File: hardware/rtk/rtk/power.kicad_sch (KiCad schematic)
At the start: 28 parts, among them J1 USB4105-GF-A, J3 B2B-PH-SM4-TBLFSN, J4 Conn_01x02_Pin, U1 BQ24075RGT, U2 TPS63020DSJR

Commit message: Schematic fixes and PCB placement start: D2, C16/18/20, J4
- D2: PRTR5V0U2X → USBLC6-2SC6 (SOT-23-6), D3 removed
- C16/C18/C20: symbol → C_Polarized_Small, footprint → 0805 HandSolder
  (T529P106M010AAE200 polymer tant 10µF 10V)
- J4: footprint assigned (PinHeader 2.54mm, on/off switch)
- rtk.kicad_pcb: initial component placement begun
- Add USBLC6-2SC6 datasheet

Co-Authored-By: Claude Sonnet 4.6 <noreply@anthropic.com>
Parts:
- J4: footprint (none) -> Connector_PinHeader_2.54mm:PinHeader_1x02_P2.54mm_Vertical
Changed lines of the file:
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@@
 			)
 		)
-		(property "Footprint" ""
+		(property "Footprint" "Connector_PinHeader_2.54mm:PinHeader_1x02_P2.54mm_Vertical"
 			(at 251.46 55.88 0)
 			(hide yes)

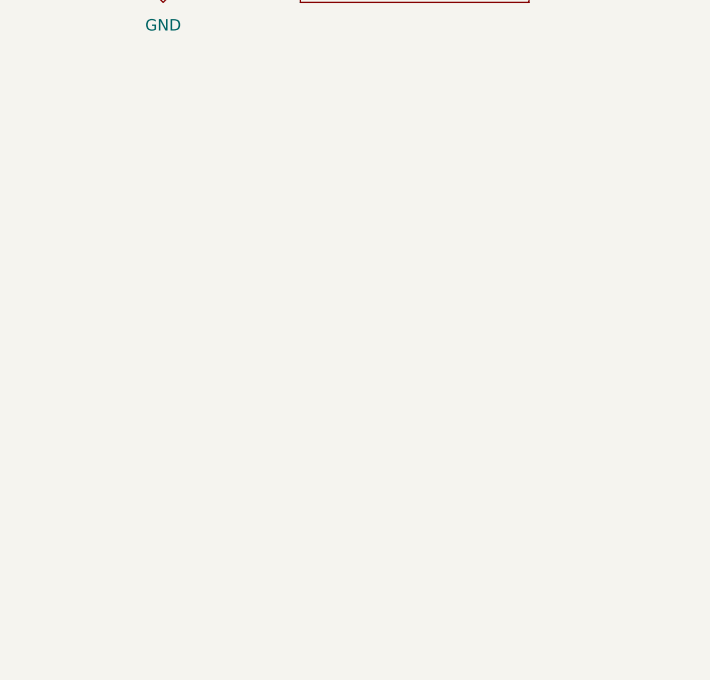
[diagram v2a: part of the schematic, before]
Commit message: Add LD3/LD4 debug LEDs: schematic, PCB placement, ioc
LD3 green PD5, LD4 red PD6 — open-drain outputs, R20/R21 1k5 pull-ups.
CubeMX regenerated with PD5/PD6 configured. Ready for routing.

Co-Authored-By: Claude Sonnet 4.6 <noreply@anthropic.com>
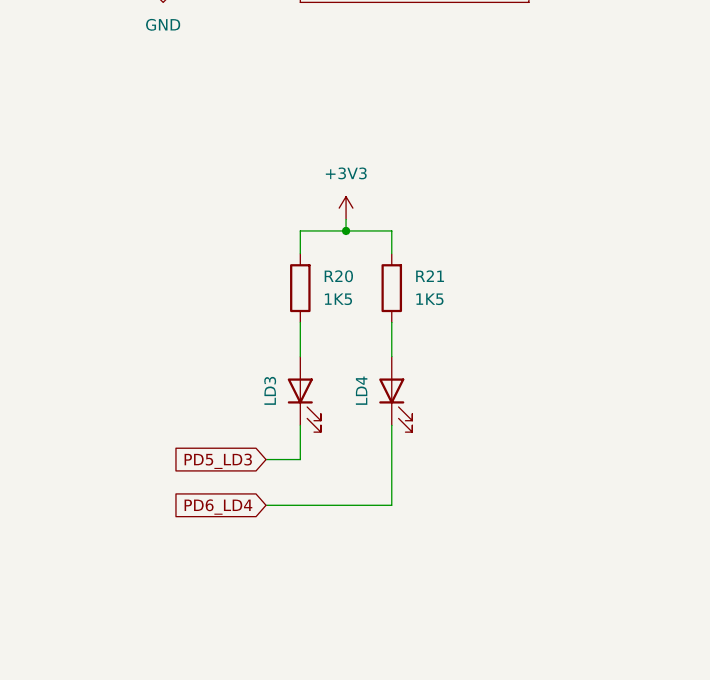
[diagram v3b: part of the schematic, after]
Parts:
- added LD3, LD4: LED, LED_SMD:LED_0805_2012Metric_Pad1.15x1.40mm_HandSolder, symbol Device:LED
- added R20, R21: 1K5, Resistor_SMD:R_0805_2012Metric_Pad1.20x1.40mm_HandSolder, symbol Device:R
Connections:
- net +3V3: now also R20.2, R21.2
- new net: LD4.2 (A), R21.1
- new net: LD3.2 (A), R20.1
- new net PD5_LD3: LD3.1 (K)
- new net PD6_LD4: LD4.1 (K)

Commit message: Add VBAT monitor: 100k divider to PA1 ADC1_IN1
Two 100k resistors divide VBAT by 2 (VBAT_2) fed to PA1. CubeMX
regenerated with ADC1 IN1 on PA1. HAL ADC driver files added.

Co-Authored-By: Claude Sonnet 4.6 <noreply@anthropic.com>
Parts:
- added R22, R23: 100K, Resistor_SMD:R_0805_2012Metric_Pad1.20x1.40mm_HandSolder, symbol Device:R
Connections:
- net GND: now also R23.2
- net VBAT: now also R22.1
- new net VBAT_2: R22.2, R23.1

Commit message: PCB: initial routing complete, pre-DRC snapshot
All signals routed including USB3300 VDD1.8 (pins 15/26 opposite sides,
long perimeter route). Ready for design rules checks.

Co-Authored-By: Claude Sonnet 4.6 <noreply@anthropic.com>
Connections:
- net VBSW: now reaches C3.1, J4.2 (Pin_2), U1.2 (BAT), U1.3 (BAT)
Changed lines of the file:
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@@
+	)
+	(junction
+		(at 204.47 53.34)
+		(diameter 0)
+		(color 0 0 0 0)
 	)
 	(junction
@@
 	(wire
 		(pts
+			(xy 204.47 53.34) (xy 229.87 53.34)
+		)
+		(stroke
+			(width 0)
+			(type default)
+		)
+	)
+	(wire
+		(pts
 			(xy 36.83 72.39) (xy 29.21 72.39)
 		)
@@
 	(wire
 		(pts
-			(xy 187.96 53.34) (xy 229.87 53.34)
+			(xy 204.47 50.8) (xy 208.28 50.8)
+		)
+		(stroke
+			(width 0)
+			(type default)
+		)
+	)
+	(wire
+		(pts
+			(xy 187.96 53.34) (xy 204.47 53.34)
 		)
 		(stroke
@@
 		(pts
 			(xy 147.32 135.89) (xy 147.32 129.54)
+		)
+		(stroke
+			(width 0)
+			(type default)
+		)
+	)
+	(wire
+		(pts
+			(xy 204.47 50.8) (xy 204.47 53.34)
 		)
 		(stroke
@@
 		)
 	)
+	(global_label "VBSW"
+		(shape input)
+		(at 208.28 50.8 0)
+		(fields_autoplaced yes)
+		(effects
+			(font
+				(size 1.27 1.27)
+			)
+			(justify left)
+		)
+		(property "Intersheetrefs" "${INTERSHEET_REFS}"
+			(at 216.2847 50.8 0)
+			(hide yes)
+			(show_name no)
+			(do_not_autoplace no)
+			(effects
+				(font
+					(size 1.27 1.27)
+				)
+				(justify left)
+			)
+		)
+	)

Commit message: BOM: replace FB2 ferrite bead with L2 bias-T inductor (LQW15AN8N0G8ZD)
Ferrite bead was wrong for the GNSS antenna bias-T RF choke — lossy
resistive impedance absorbs signal. Replaced with Murata 8.0nH wire-wound
inductor (0402). Schematic and PCB updated with new symbol/footprint.

Co-Authored-By: Claude Sonnet 4.6 <noreply@anthropic.com>
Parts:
- added H1, H2, H3, H4: MountingHole, MountingHole:MountingHole_2.7mm, symbol Mechanical:MountingHole
- added TP1: TestPoint, Connector_PinHeader_2.54mm:PinHeader_1x01_P2.54mm_Vertical, symbol Connector:TestPoint
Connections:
- net at U2.14 (PG): now also TP1.1
- no-connect marks 5 -> 4
